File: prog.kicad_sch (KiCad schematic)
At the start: 8 parts, among them J3 USB_C_Receptacle_USB2.0_16P, U2 FT231XS

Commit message: USB caps
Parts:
- added C2, C3: 4.7uF, Capacitor_SMD:C_0402_1005Metric, symbol Device:C
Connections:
- net +5VUSB: now also U2.15 (VCC), U2.3 (VCCIO), C2.1, C3.1
- net GND: now also C2.2, C3.2
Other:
- moved on the sheet: FB1

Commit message: Usb programme
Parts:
- added C4, C6: 100nF, Capacitor_SMD:C_0402_1005Metric, symbol Device:C
- added C5: 10nF, Capacitor_SMD:C_0402_1005Metric, symbol Device:C
- added D1: Red LED, LED_SMD:LED_0603_1608Metric, symbol Device:LED
- added D2: Blue LED, LED_SMD:LED_0603_1608Metric, symbol Device:LED
- added Q1: MUN5211T1G, Package_TO_SOT_SMD:SOT-323_SC-70, symbol Transistor_BJT:Q_NPN_BEC
- added R10, R8, R9: 100k, Resistor_SMD:R_0402_1005Metric, symbol Device:R
- added R5, R6: 240R, Resistor_SMD:R_0402_1005Metric, symbol Device:R
- added R7: 470k, Resistor_SMD:R_0402_1005Metric, symbol Device:R
- added U3, U4: 74LVC1G126, Package_TO_SOT_SMD:SOT-353_SC-70-5, symbol 74xGxx:74LVC1G126
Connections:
- net +5VUSB: now also R5.2; no longer U2.3 (VCCIO)
- net GND: now also C4.1, C6.1, Q1.2 (E), R7.2, R8.1, R9.1, U3.3 (GND), U4.3 (GND)
- net DTR: now reaches U2.1 (~{DTR})
- net DTR: now also C5.1
- net TXDEN: now reaches U2.10 (CBUS2)
- net TXDEN: now also R9.2, U4.1
- net VCCIO: now reaches U2.13 (3V3OUT)
- net VCCIO: now also U2.14 (~{RESET}), U2.3 (VCCIO), C4.2, C6.2, R10.2, U3.5 (VCC), U4.5 (VCC)
- net SLEEP: now reaches U2.17 (CBUS1)
- net SLEEP: now also R8.2, U3.1
- net at U2.18 (CBUS0): now also D1.1 (K)
- net at U2.19 (CBUS3): now also D2.1 (K)
- net RTS: now reaches U2.2 (~{RTS})
- net FT_TX: now reaches U2.20 (TXD)
- net FT_TX: now also U4.2
- net FT_RX: now reaches U2.4 (RXD)
- net FT_RX: now also U3.4
- new net: C5.2, Q1.1 (B)
- new net: D1.2 (A), D2.2 (A), R5.1
- new net: R6.2, U3.2
- new net RESn: Q1.3 (C)
- new net RX: R6.1, R7.1
- new net TX: R10.1, U4.4
- no-connect marks 2 -> 6
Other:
- note added: "RX tri-state"
- note added: "TX tri-state"
- note added: "idle high"
- note added: "~20uS reset pulse"

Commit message: sch, pcb: update pn fields
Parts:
- C1, C5: value 10nF -> 10nF 16v; Part Number (none) -> GRM155R71C103KA01D
- C2, C3: value 4.7uF -> 4.7uF 10v; Part Number (none) -> GRM155R61A475MEAAD
- C4, C6: value 100nF -> 100nF 16v; Part Number (none) -> GRM155R71C104KA88D
- D1: Part Number (none) -> 150060RS75000
- D2: Part Number (none) -> 150060BS75000
- FB1: Part Number (none) -> MPZ1608S221ATA00
- J3: Part Number (none) -> USB4105-GF-A
- Q1: Part Number (none) -> MUN5211T1G
- R1, R2: Part Number (none) -> RC0402FR-075K1L
- R10, R8, R9: Part Number (none) -> RC0402FR-07100KL
- R3, R4: Part Number (none) -> RC0402FR-0727RL
- R5, R6: Part Number (none) -> RC0402FR-07240RL
- R7: Part Number (none) -> RC0402FR-07470KL
- U2: Part Number (none) -> FT231XS-R
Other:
- moved on the sheet: C1, C2, R9

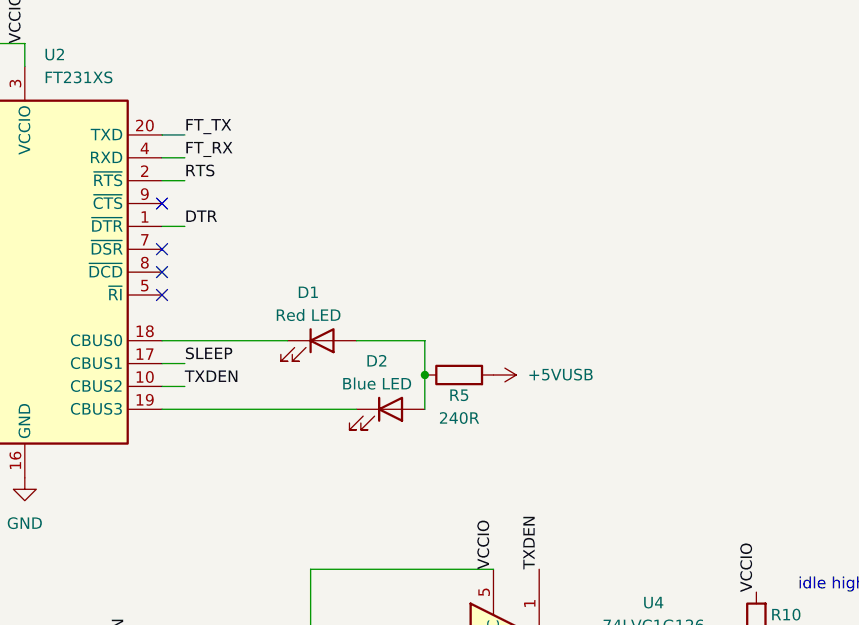
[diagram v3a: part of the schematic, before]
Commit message: prog, pcb: test points
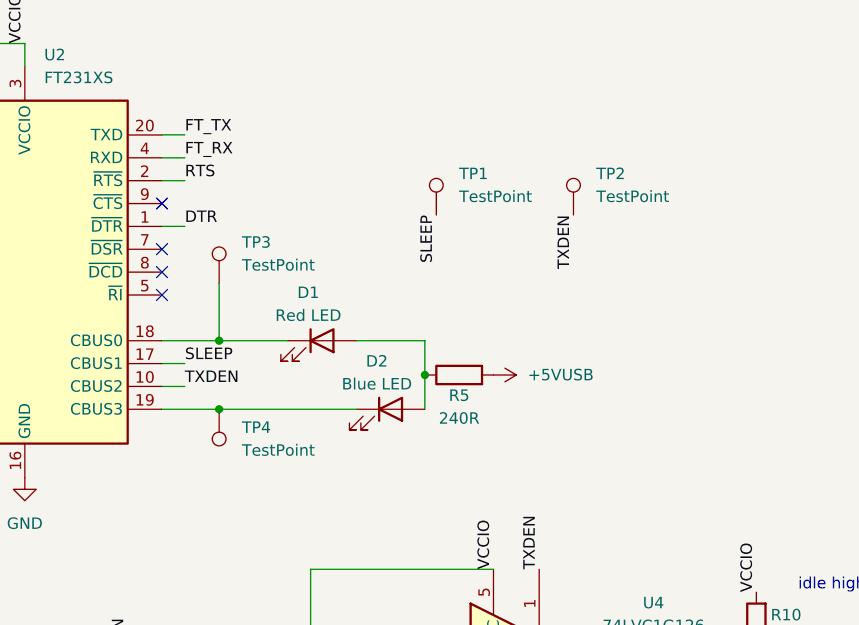
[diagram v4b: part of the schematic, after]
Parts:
- added TP1, TP2, TP3, TP4: TestPoint, TestPoint:TestPoint_Pad_D1.0mm, symbol Connector:TestPoint
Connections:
- net SLEEP: now also TP1.1
- net TXDEN: now also TP2.1
- net at D1.1 (K), U2.18 (CBUS0): now also TP3.1
- net at D2.1 (K), U2.19 (CBUS3): now also TP4.1

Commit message: sch, pcb: add part numbers
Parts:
- TP1, TP2, TP3, TP4: now left out of the parts list
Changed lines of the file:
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@@
 		(unit 1)
 		(exclude_from_sim no)
-		(in_bom yes)
+		(in_bom no)
 		(on_board yes)
 		(dnp no)
@@
 		(unit 1)
 		(exclude_from_sim no)
-		(in_bom yes)
+		(in_bom no)
 		(on_board yes)
 		(dnp no)
@@
 		(unit 1)
 		(exclude_from_sim no)
-		(in_bom yes)
+		(in_bom no)
 		(on_board yes)
 		(dnp no)
@@
 		(unit 1)
 		(exclude_from_sim no)
-		(in_bom yes)
-		(on_board yes)
-		(dnp no)
+		(in_bom no)
+		(on_board yes)
+		(dnp no)

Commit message: sch: erc
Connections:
- net RTS: no longer names the net of U2.2 (~{RTS})
- no-connect marks 6 -> 7
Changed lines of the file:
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@@
 	)
 	(junction
+		(at 76.2 40.64)
+		(diameter 0)
+		(color 0 0 0 0)
+	)
+	(junction
 		(at 160.02 106.68)
 		(diameter 0)
@@
 		(color 0 0 0 0)
 	)
+	(junction
+		(at 85.09 77.47)
+		(diameter 0)
+		(color 0 0 0 0)
+	)
 	(no_connect
 		(at 153.67 99.06)
@@
 	)
 	(no_connect
+		(at 153.67 88.9)
+	)
+	(no_connect
 		(at 153.67 91.44)
 	)
@@
 	(wire
 		(pts
-			(xy 153.67 88.9) (xy 156.21 88.9)
-		)
-		(stroke
-			(width 0)
-			(type default)
-		)
-	)
-	(wire
-		(pts
 			(xy 99.06 91.44) (xy 118.11 91.44)
 		)
@@
 	(wire
 		(pts
+			(xy 76.2 40.64) (xy 71.12 40.64)
+		)
+		(stroke
+			(width 0)
+			(type default)
+		)
+	)
+	(wire
+		(pts
+			(xy 85.09 77.47) (xy 83.82 77.47)
+		)
+		(stroke
+			(width 0)
+			(type default)
+		)
+	)
+	(wire
+		(pts
 			(xy 153.67 109.22) (xy 156.21 109.22)
 		)
@@
 	(wire
 		(pts
-			(xy 86.36 77.47) (xy 83.82 77.47)
+			(xy 87.63 77.47) (xy 85.09 77.47)
 		)
 		(stroke
@@
 	(wire
 		(pts
+			(xy 78.74 40.64) (xy 76.2 40.64)
+		)
+		(stroke
+			(width 0)
+			(type default)
+		)
+	)
+	(wire
+		(pts
+			(xy 85.09 73.66) (xy 85.09 77.47)
+		)
+		(stroke
+			(width 0)
+			(type default)
+		)
+	)
+	(wire
+		(pts
 			(xy 182.88 110.49) (xy 182.88 114.3)
 		)
@@
 		)
 	)
-	(label "RTS"
-		(at 156.21 88.9 0)
-		(effects
-			(font
-				(size 1.27 1.27)
-			)
-			(justify left bottom)
-		)
-	)
 	(label "VCCIO"
 		(at 219.71 134.62 90)
@@
 	)
 	(symbol
+		(lib_id "power:PWR_FLAG")
+		(at 76.2 40.64 0)
+		(unit 1)
+		(exclude_from_sim no)
+		(in_bom yes)
+		(on_board yes)
+		(dnp no)
+		(fields_autoplaced yes)
+		(property "Reference" "#FLG06"
+			(at 76.2 38.735 0)
+			(effects
+				(font
+					(size 1.27 1.27)
+				)
+				(hide yes)
+			)
+		)
+		(property "Value" "PWR_FLAG"
+			(at 76.2 35.56 0)
+			(effects
+				(font
+					(size 1.27 1.27)
+				)
+			)
+		)
+		(property "Footprint" ""
+			(at 76.2 40.64 0)
+			(effects
+				(font
+					(size 1.27 1.27)
+				)
+				(hide yes)
+			)
+		)
+		(property "Datasheet" "~"
+			(at 76.2 40.64 0)
+			(effects
+				(font
+					(size 1.27 1.27)
+				)
+				(hide yes)
+			)
+		)
+		(property "Description" "Special symbol for telling ERC where power comes from"
+			(at 76.2 40.64 0)
+			(effects
+				(font
+					(size 1.27 1.27)
+				)
+				(hide yes)
+			)
+		)
+		(pin "1"
+		)
+		(instances
+			(project "P2 Kevinbot Board"
+				(path "/362ca48c-0b77-4943-b8b3-fc15ab97f30d/36ef8cf2-6197-4fa1-9b06-a24478d77804/021ef78a-1e6a-4c77-a259-f094daf2e0e2"
+					(reference "#FLG06")
+					(unit 1)
+				)
+			)
+		)
+	)
+	(symbol
 		(lib_id "Device:R")
 		(at 121.92 147.32 180)
@@
 	(symbol
 		(lib_id "power:VBUS")
-		(at 86.36 77.47 0)
+		(at 87.63 77.47 0)
 		(unit 1)
 		(exclude_from_sim no)
@@
 		(dnp no)
 		(property "Reference" "#PWR03"
-			(at 86.36 81.28 0)
+			(at 87.63 81.28 0)
 			(effects
 				(font
@@
 		)
 		(property "Value" "VBUS"
-			(at 84.074 73.914 0)
+			(at 85.344 73.914 0)
 			(effects
 				(font
@@
 		)
 		(property "Footprint" ""
-			(at 86.36 77.47 0)
+			(at 87.63 77.47 0)
 			(effects
 				(font
@@
 		)
 		(property "Datasheet" ""
-			(at 86.36 77.47 0)
+			(at 87.63 77.47 0)
 			(effects
 				(font
@@
 		)
 		(property "Description" "Power symbol creates a global label with name \"VBUS\""
-			(at 86.36 77.47 0)
+			(at 87.63 77.47 0)
 			(effects
 				(font
@@
 	)
 	(symbol
+		(lib_id "power:PWR_FLAG")
+		(at 85.09 73.66 0)
+		(unit 1)
+		(exclude_from_sim no)
+		(in_bom yes)
+		(on_board yes)
+		(dnp no)
+		(fields_autoplaced yes)
+		(property "Reference" "#FLG05"
+			(at 85.09 71.755 0)
+			(effects
+				(font
+					(size 1.27 1.27)
+				)
+				(hide yes)
+			)
+		)
+		(property "Value" "PWR_FLAG"
+			(at 85.09 68.58 0)
+			(effects
+				(font
+					(size 1.27 1.27)
+				)
+			)
+		)
+		(property "Footprint" ""
+			(at 85.09 73.66 0)
+			(effects
+				(font
+					(size 1.27 1.27)
+				)
+				(hide yes)
+			)
+		)
+		(property "Datasheet" "~"
+			(at 85.09 73.66 0)
+			(effects
+				(font
+					(size 1.27 1.27)
+				)
+				(hide yes)
+			)
+		)
+		(property "Description" "Special symbol for telling ERC where power comes from"
+			(at 85.09 73.66 0)
+			(effects
+				(font
+					(size 1.27 1.27)
+				)
+				(hide yes)
+			)
+		)
+		(pin "1"
+		)
+		(instances
+			(project ""
+				(path "/362ca48c-0b77-4943-b8b3-fc15ab97f30d/36ef8cf2-6197-4fa1-9b06-a24478d77804/021ef78a-1e6a-4c77-a259-f094daf2e0e2"
+					(reference "#FLG05")
+					(unit 1)
+				)
+			)
+		)
+	)
+	(symbol
 		(lib_id "power:GND")
 		(at 92.71 151.13 0)
@@
 	(symbol
 		(lib_id "power:+5VD")
-		(at 71.12 40.64 270)
+		(at 78.74 40.64 270)
 		(unit 1)
 		(exclude_from_sim no)
@@
 		(fields_autoplaced yes)
 		(property "Reference" "#PWR099"
-			(at 67.31 40.64 0)
+			(at 74.93 40.64 0)
 			(effects
 				(font
@@
 		)
 		(property "Value" "+5VUSB"
-			(at 74.93 40.6399 90)
+			(at 82.55 40.6399 90)
 			(effects
 				(font
@@
 		)
 		(property "Footprint" ""
-			(at 71.12 40.64 0)
+			(at 78.74 40.64 0)
 			(effects
 				(font
@@
 		)
 		(property "Datasheet" ""
-			(at 71.12 40.64 0)
+			(at 78.74 40.64 0)
 			(effects
 				(font
@@
 		)
 		(property "Description" "Power symbol creates a global label with name \"+5VD\""
-			(at 71.12 40.64 0)
+			(at 78.74 40.64 0)
 			(effects
 				(font
